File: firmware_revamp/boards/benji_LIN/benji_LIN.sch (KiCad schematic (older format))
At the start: 34 parts, among them J1 CONN_02X03, U1 MCP2561-E_SN, U101 TPS560430YF, U2 ATMEGA16M1, Y1 Crystal_SMD

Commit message: Added resistors to programming header, added 12V_Protected
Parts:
- removed C? (x2): C_100nF, footprints:C_0603_1608Metric, symbol formula:C_100nF
- removed D?: BAS40-00, Package_TO_SOT_SMD:SOT-23, symbol formula:BAS40-00
- added C6, C7: C_0.1uF, footprints:C_0805_OEM, symbol formula:C_0.1uF
- added D1: Diode_600V_1A_SM, footprints:Diode_600V_1A_SM, symbol formula:Diode_600V_1A_SM
- added R? (x3): R_330, footprints:R_0805_OEM, symbol formula:R_330
- COUT102: footprint footprints:Fuse_1812 -> footprints:C_1812_OEM
- U101: footprint footprints:SOT-23-6_OEM -> Package_TO_SOT_SMD:SOT-23-6_Handsoldering
- gave numbers to parts that had none: 2
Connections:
- net labels added: 12V_Protected, CAN_+, CAN_-
- net labels removed: CAN_HI, CAN_LO
- wire segments 87 -> 101
- no-connect marks 3 -> 24
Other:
- moved on the sheet: C1, D101, D102, F101, J1, R101, R2, R4, U1, U3

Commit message: added test points
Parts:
- gave numbers to parts that had none: 3
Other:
- note added: "TEST POINTS"
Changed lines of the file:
@@
-$EndComp
-$Comp
-L template-rescue:R_100K-formula R103
-U 1 1 5BEE2A52
-P 4500 8150
-F 0 "R103" V 4600 8100 50  0000 L CNN
-F 1 "R_100K" V 4400 8000 50  0000 L CNN
-F 2 "footprints:R_0805_OEM" H 4430 8150 50  0001 C CNN
-F 3 "https://industrial.panasonic.com/cdbs/www-data/pdf/RDA0000/AOA0000C304.pdf" H 4580 8150 50  0001 C CNN
-F 4 "DK" H 4500 8150 60  0001 C CNN "MFN"
-F 5 "P100KCCT-ND" H 4500 8150 60  0001 C CNN "MPN"
-F 6 "https://www.digikey.com/product-detail/en/panasonic-electronic-components/ERJ-6ENF1003V/P100KCCT-ND/119551" H 4980 8550 60  0001 C CNN "PurchasingLink"
-	1    4500 8150
-	0    1    1    0
-$EndComp
-$Comp
-L template-rescue:C_0.1uF-formula C103
-U 1 1 5BEE239B
-P 4500 7300
-F 0 "C103" V 4440 7440 50  0000 C CNN
-F 1 "C_0.1uF" V 4540 7500 50  0000 C CNN
-F 2 "footprints:C_0805_OEM" H 4538 7150 50  0001 C CNN
-F 3 "http://datasheets.avx.com/X7RDielectric.pdf" H 4525 7400 50  0001 C CNN
-F 4 "DK" H 4500 7300 60  0001 C CNN "MFN"
-F 5 "478-3352-1-ND" H 4500 7300 60  0001 C CNN "MPN"
-F 6 "https://www.digikey.com/products/en?keywords=478-3352-1-ND" H 4925 7800 60  0001 C CNN "PurchasingLink"
-	1    4500 7300
-	0    -1   -1   0
 $EndComp
 $Comp
@@
 	1    0    0    -1
 $EndComp
-Text Notes 3950 8400 0    50   ~ 0
-Feedback Divider\n
-Text Notes 4100 7150 0    50   ~ 0
-Bootstrap Capacitor\n
 Text Notes 5400 7200 0    50   ~ 0
 Output Capacitors\n
@@
 Text Notes 3550 4900 0    89   ~ 0
 16 MHz CRYSTAL\n
-Text Notes 12050 7200 0    89   ~ 0
+Text Notes 12450 7200 0    89   ~ 0
 POWER FLAGS\n
 $Comp
@@
 Wire Wire Line
 	4750 7300 4750 7450
-Wire Wire Line
-	4000 7450 4750 7450
-Connection ~ 4750 7450
 Wire Wire Line
 	4750 7450 4800 7450
@@
 RESET
 $Comp
-L formula:R_330 R?
+L formula:R_330 R7
 U 1 1 602CA042
 P 14350 4500
-F 0 "R?" V 14143 4500 50  0000 C CNN
+F 0 "R7" V 14143 4500 50  0000 C CNN
 F 1 "R_330" V 14234 4500 50  0000 C CNN
 F 2 "footprints:R_0805_OEM" H 14280 4500 50  0001 C CNN
@@
 	14500 4500 14600 4500
 $Comp
-L formula:R_330 R?
+L formula:R_330 R6
 U 1 1 602D41EE
 P 13300 4400
-F 0 "R?" V 13093 4400 50  0000 C CNN
+F 0 "R6" V 13093 4400 50  0000 C CNN
 F 1 "R_330" V 13184 4400 50  0000 C CNN
 F 2 "footprints:R_0805_OEM" H 13230 4400 50  0001 C CNN
@@
 	13400 4600 13600 4600
 $Comp
-L formula:R_330 R?
+L formula:R_330 R5
 U 1 1 602DEDF9
 P 13150 4700
-F 0 "R?" V 12943 4700 50  0000 C CNN
+F 0 "R5" V 12943 4700 50  0000 C CNN
 F 1 "R_330" V 13034 4700 50  0000 C CNN
 F 2 "footprints:R_0805_OEM" H 13080 4700 50  0001 C CNN
@@
 NoConn ~ 3650 1100
 NoConn ~ 3650 1000
+Connection ~ 4750 7450
+Wire Wire Line
+	4000 7450 4750 7450
+Text Notes 4100 7150 0    50   ~ 0
+Bootstrap Capacitor\n
+Text Notes 3950 8400 0    50   ~ 0
+Feedback Divider\n
+$Comp
+L template-rescue:C_0.1uF-formula C103
+U 1 1 5BEE239B
+P 4500 7300
+F 0 "C103" V 4440 7440 50  0000 C CNN
+F 1 "C_0.1uF" V 4540 7500 50  0000 C CNN
+F 2 "footprints:C_0805_OEM" H 4538 7150 50  0001 C CNN
+F 3 "http://datasheets.avx.com/X7RDielectric.pdf" H 4525 7400 50  0001 C CNN
+F 4 "DK" H 4500 7300 60  0001 C CNN "MFN"
+F 5 "478-3352-1-ND" H 4500 7300 60  0001 C CNN "MPN"
+F 6 "https://www.digikey.com/products/en?keywords=478-3352-1-ND" H 4925 7800 60  0001 C CNN "PurchasingLink"
+	1    4500 7300
+	0    -1   -1   0
+$EndComp
+$Comp
+L template-rescue:R_100K-formula R103
+U 1 1 5BEE2A52
+P 4500 8150
+F 0 "R103" V 4600 8100 50  0000 L CNN
+F 1 "R_100K" V 4400 8000 50  0000 L CNN
+F 2 "footprints:R_0805_OEM" H 4430 8150 50  0001 C CNN
+F 3 "https://industrial.panasonic.com/cdbs/www-data/pdf/RDA0000/AOA0000C304.pdf" H 4580 8150 50  0001 C CNN
+F 4 "DK" H 4500 8150 60  0001 C CNN "MFN"
+F 5 "P100KCCT-ND" H 4500 8150 60  0001 C CNN "MPN"
+F 6 "https://www.digikey.com/product-detail/en/panasonic-electronic-components/ERJ-6ENF1003V/P100KCCT-ND/119551" H 4980 8550 60  0001 C CNN "PurchasingLink"
+	1    4500 8150
+	0    1    1    0
+$EndComp
+Text Label 13550 7650 0    50   ~ 0
+12V_Protected
+$Comp
+L power:PWR_FLAG #FLG?
+U 1 1 603FB834
+P 13550 7500
+F 0 "#FLG?" H 13550 7575 50  0001 C CNN
+F 1 "PWR_FLAG" H 13550 7674 50  0000 C CNN
+F 2 "" H 13550 7500 50  0001 C CNN
+F 3 "~" H 13550 7500 50  0001 C CNN
+	1    13550 7500
+	1    0    0    -1
+$EndComp
+Wire Wire Line
+	13550 7500 13550 7650
+Text Notes 12500 6000 0    89   ~ 0
+TEST POINTS
+Text Label 12000 6200 0    50   ~ 0
+12V_Protected
+Text Label 12650 6200 0    50   ~ 0
+GND
+Text Label 12900 6200 0    50   ~ 0
+5V
+Text Label 13100 6200 0    50   ~ 0
+CAN_+
+Text Label 13400 6200 0    50   ~ 0
+CAN_-
+Text Label 13700 6200 0    50   ~ 0
+LIN_BUS
 $EndSCHEMATC

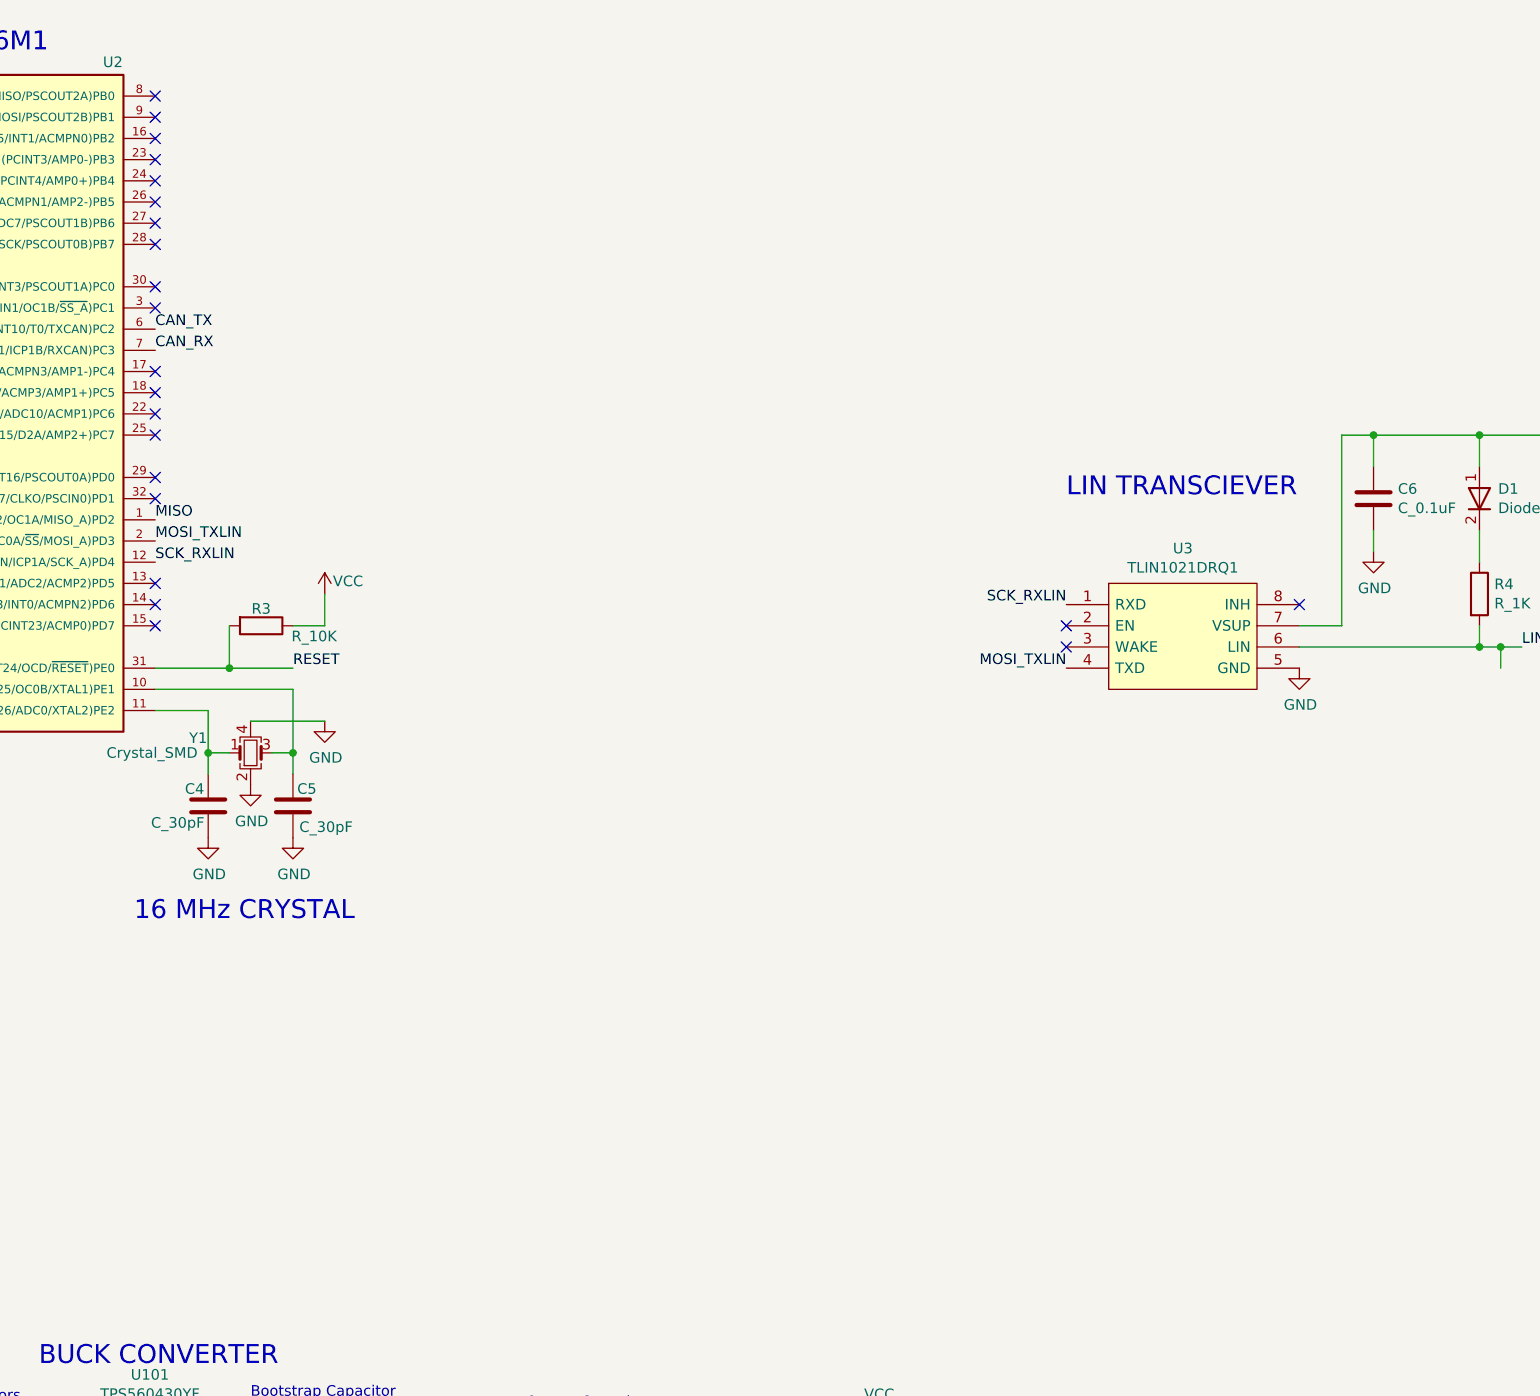
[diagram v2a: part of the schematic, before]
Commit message: add debug leds
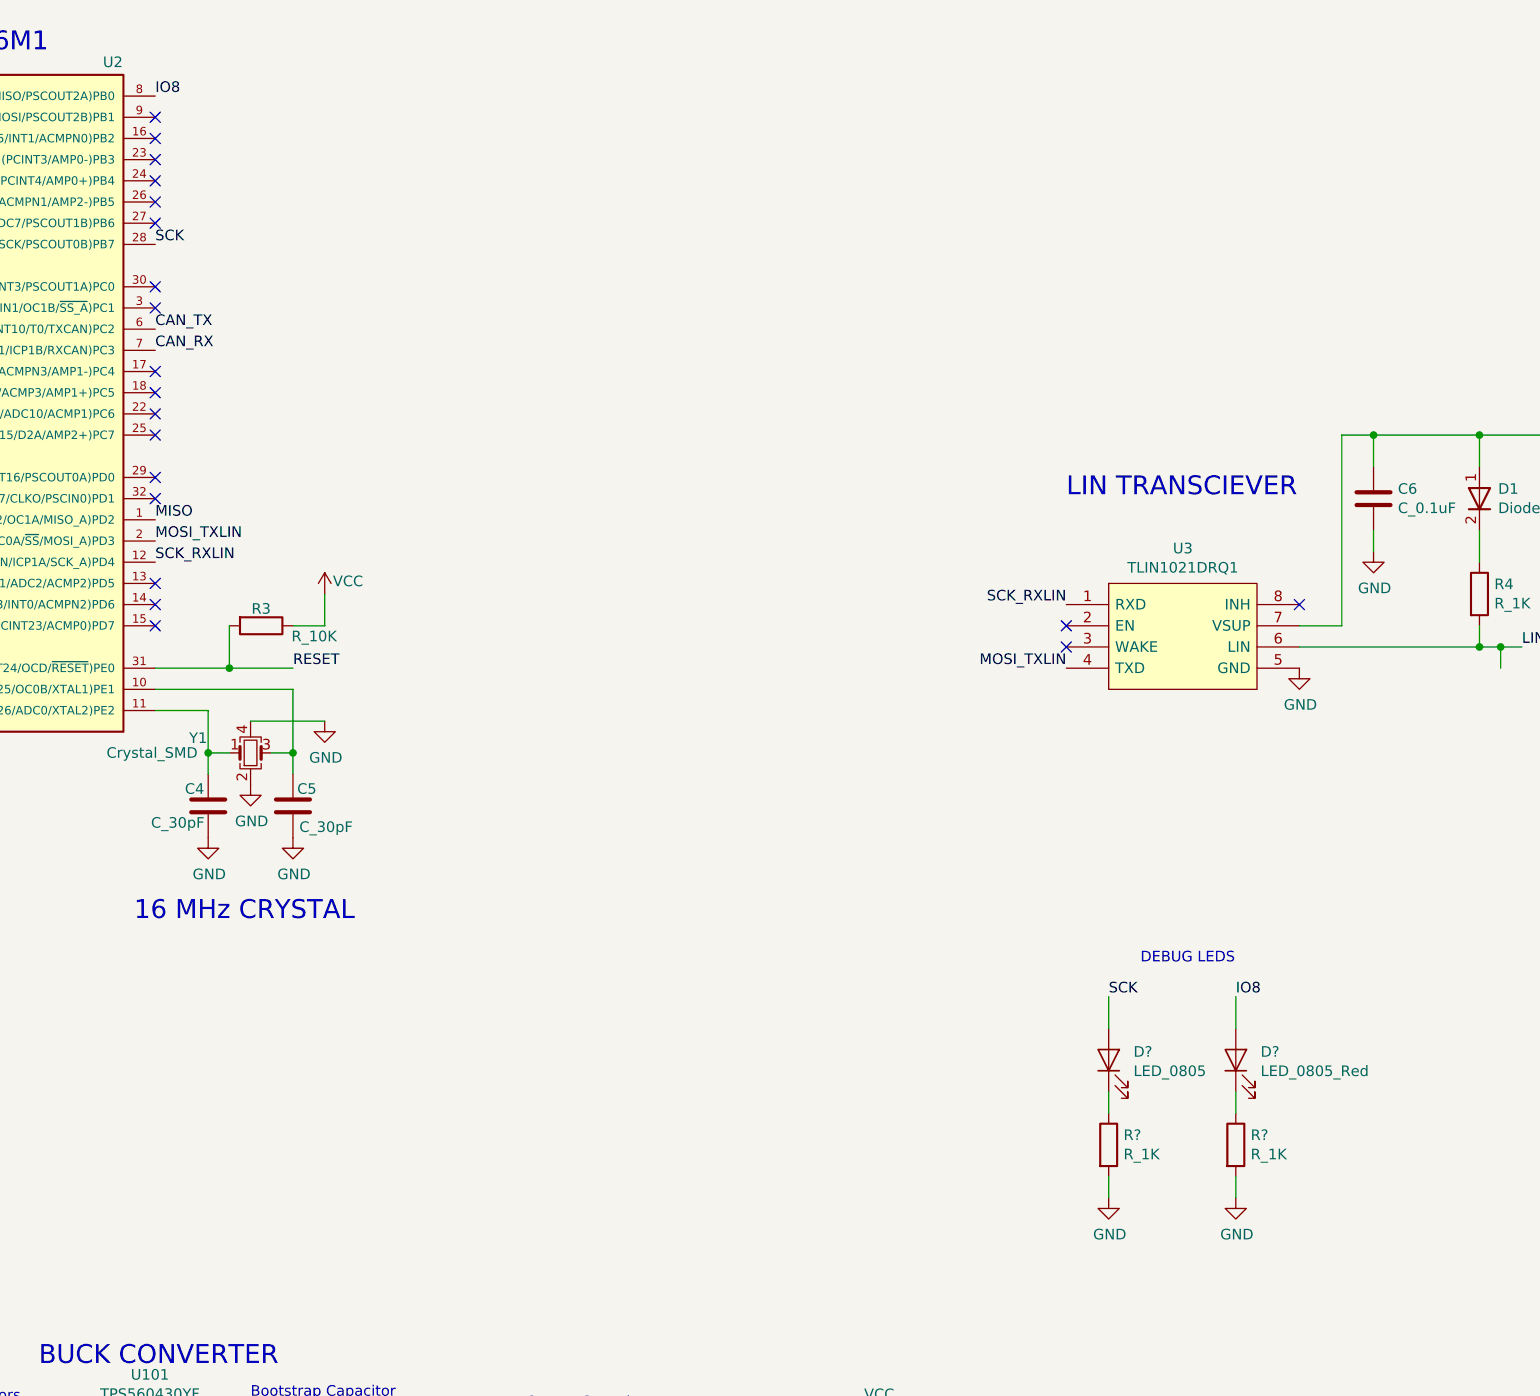
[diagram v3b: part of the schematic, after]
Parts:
- added D?: LED_0805, footprints:LED_0805_OEM, symbol formula:LED_0805
- added D?: LED_0805_Red, footprints:LED_0805_OEM, symbol formula:LED_0805_Red
- added R? (x2): R_1K, footprints:R_0805_OEM, symbol formula:R_1K
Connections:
- net GND: now also R?.2, R?.2
- net SCK: now reaches U2.28 ((PCINT7/ADC4/SCK/PSCOUT0B)PB7)
- net SCK: now also D?.2 (A)
- net IO8: now reaches U2.8 ((PCINT0/MISO/PSCOUT2A)PB0)
- net IO8: now also D?.2 (A)
- new net: D?.1 (K), R?.1 (x2)
- no-connect marks 24 -> 22
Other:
- note added: "DEBUG LEDS"
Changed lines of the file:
@@
 NoConn ~ 3650 2000
 NoConn ~ 3650 1900
-NoConn ~ 3650 1700
 NoConn ~ 3650 1600
 NoConn ~ 3650 1500
@@
 NoConn ~ 3650 1200
 NoConn ~ 3650 1100
-NoConn ~ 3650 1000
 Connection ~ 4750 7450
 Wire Wire Line
@@
 12V_Protected
 $Comp
-L power:PWR_FLAG #FLG?
+L power:PWR_FLAG #FLG0101
 U 1 1 603FB834
 P 13550 7500
-F 0 "#FLG?" H 13550 7575 50  0001 C CNN
+F 0 "#FLG0101" H 13550 7575 50  0001 C CNN
 F 1 "PWR_FLAG" H 13550 7674 50  0000 C CNN
 F 2 "" H 13550 7500 50  0001 C CNN
@@
 Text Label 13700 6200 0    50   ~ 0
 LIN_BUS
+Text Notes 8300 5100 0    50   ~ 0
+DEBUG LEDS
+Text Label 3650 1700 0    50   ~ 0
+SCK
+Text Label 3650 1000 0    50   ~ 0
+IO8
+Text Label 8150 5250 0    50   ~ 0
+SCK
+Text Label 8750 5250 0    50   ~ 0
+IO8
+$Comp
+L formula:LED_0805 D?
+U 1 1 60323BBE
+P 8150 5550
+F 0 "D?" V 8189 5433 50  0000 R CNN
+F 1 "LED_0805" V 8098 5433 50  0000 R CNN
+F 2 "footprints:LED_0805_OEM" H 8050 5550 50  0001 C CNN
+F 3 "http://www.osram-os.com/Graphics/XPic9/00078860_0.pdf" H 8150 5650 50  0001 C CNN
+F 4 "DK" H 8150 5550 60  0001 C CNN "MFN"
+F 5 "475-1410-1-ND" H 8150 5550 60  0001 C CNN "MPN"
+F 6 "https://www.digikey.com/products/en?keywords=475-1410-1-ND" H 8550 6050 60  0001 C CNN "PurchasingLink"
+	1    8150 5550
+	0    -1   -1   0
+$EndComp
+Wire Wire Line
+	8150 5400 8150 5250
+$Comp
+L formula:LED_0805_Red D?
+U 1 1 60327C95
+P 8750 5550
+F 0 "D?" V 8789 5433 50  0000 R CNN
+F 1 "LED_0805_Red" V 8698 5433 50  0000 R CNN
+F 2 "footprints:LED_0805_OEM" H 8650 5550 50  0001 C CNN
+F 3 "http://www.osram-os.com/Graphics/XPic8/00078869_0.pdf" H 8750 5650 50  0001 C CNN
+F 4 "DK" H 8750 5550 60  0001 C CNN "MFN"
+F 5 "475-1415-1-ND" H 8750 5550 60  0001 C CNN "MPN"
+F 6 "https://www.digikey.com/product-detail/en/osram-opto-semiconductors-inc/LH-R974-LP-1/475-1415-1-ND/1802604" H 9150 6050 60  0001 C CNN "PurchasingLink"
+	1    8750 5550
+	0    -1   -1   0
+$EndComp
+Wire Wire Line
+	8750 5250 8750 5400
+$Comp
+L formula:R_1K R?
+U 1 1 6032BF02
+P 8150 5950
+F 0 "R?" H 8220 5996 50  0000 L CNN
+F 1 "R_1K" H 8220 5905 50  0000 L CNN
+F 2 "footprints:R_0805_OEM" H 8080 5950 50  0001 C CNN
+F 3 "https://www.seielect.com/Catalog/SEI-rncp.pdf" H 8230 5950 50  0001 C CNN
+F 4 "DK" H 8150 5950 60  0001 C CNN "MFN"
+F 5 "RNCP0805FTD1K00CT-ND" H 8150 5950 60  0001 C CNN "MPN"
+F 6 "https://www.digikey.com/products/en?keywords=RNCP0805FTD1K00CT-ND" H 8630 6350 60  0001 C CNN "PurchasingLink"
+	1    8150 5950
+	1    0    0    -1
+$EndComp
+$Comp
+L formula:R_1K R?
+U 1 1 6032C9E2
+P 8750 5950
+F 0 "R?" H 8820 5996 50  0000 L CNN
+F 1 "R_1K" H 8820 5905 50  0000 L CNN
+F 2 "footprints:R_0805_OEM" H 8680 5950 50  0001 C CNN
+F 3 "https://www.seielect.com/Catalog/SEI-rncp.pdf" H 8830 5950 50  0001 C CNN
+F 4 "DK" H 8750 5950 60  0001 C CNN "MFN"
+F 5 "RNCP0805FTD1K00CT-ND" H 8750 5950 60  0001 C CNN "MPN"
+F 6 "https://www.digikey.com/products/en?keywords=RNCP0805FTD1K00CT-ND" H 9230 6350 60  0001 C CNN "PurchasingLink"
+	1    8750 5950
+	1    0    0    -1
+$EndComp
+Wire Wire Line
+	8150 5700 8150 5800
+Wire Wire Line
+	8750 5700 8750 5800
+$Comp
+L power:GND #PWR?
+U 1 1 60332FFA
+P 8150 6200
+F 0 "#PWR?" H 8150 5950 50  0001 C CNN
+F 1 "GND" H 8155 6027 50  0000 C CNN
+F 2 "" H 8150 6200 50  0001 C CNN
+F 3 "" H 8150 6200 50  0001 C CNN
+	1    8150 6200
+	1    0    0    -1
+$EndComp
+Wire Wire Line
+	8150 6200 8150 6100
+$Comp
+L power:GND #PWR?
+U 1 1 6033649C
+P 8750 6200
+F 0 "#PWR?" H 8750 5950 50  0001 C CNN
+F 1 "GND" H 8755 6027 50  0000 C CNN
+F 2 "" H 8750 6200 50  0001 C CNN
+F 3 "" H 8750 6200 50  0001 C CNN
+	1    8750 6200
+	1    0    0    -1
+$EndComp
+Wire Wire Line
+	8750 6200 8750 6100
 $EndSCHEMATC
